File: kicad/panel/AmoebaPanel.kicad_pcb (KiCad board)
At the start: 2 copper layers, 127.8 x 100 mm, 204 parts, among them J1 Conn_01x01_Pin, J10 Conn_01x01_Pin, J11 Conn_01x01_Pin, J12 Conn_01x01_Pin, J13 Conn_01x01_Pin, J14 Conn_01x01_Pin, J15 Conn_01x01_Pin, J16 Conn_01x01_Pin, J17 Conn_01x01_Pin, J18 Conn_01x01_Pin, J19 Conn_01x01_Pin, J2 Conn_01x01_Pin, J20 Conn_01x01_Pin, J21 Conn_01x01_Pin, J22 Conn_01x01_Pin, J23 Conn_01x01_Pin, J24 Conn_01x01_Pin, J25 Conn_01x01_Pin, J26 Conn_01x01_Pin, J27 Conn_01x01_Pin, J28 Conn_01x01_Pin, J29 Conn_01x01_Pin, J3 Conn_01x01_Pin, J30 Conn_01x01_Pin, J31 Conn_01x01_Pin, J32 Conn_01x01_Pin, J33 Conn_01x01_Pin, J34 Conn_01x01_Pin, J35 Conn_01x01_Pin, J36 Conn_01x01_Pin, J37 Conn_01x01_Pin, J38 Conn_01x01_Pin, J39 Conn_01x01_Pin, J4 Conn_01x01_Pin, J40 Conn_01x01_Pin, J41 Conn_01x01_Pin, J42 Conn_01x01_Pin, J43 Conn_01x01_Pin, J44 Conn_01x01_Pin, J45 Conn_01x01_Pin, J46 Conn_01x01_Pin, J47 Conn_01x01_Pin, J48 Conn_01x01_Pin, J49 Conn_01x01_Pin, J5 Conn_01x01_Pin, J50 Conn_01x01_Pin, J51 Conn_01x01_Pin, J52 Conn_01x01_Pin, J53 Conn_01x01_Pin, J54 Conn_01x01_Pin, J55 Conn_01x01_Pin, J56 Conn_01x01_Pin, J57 Conn_01x01_Pin, J58 Conn_01x01_Pin, J59 Conn_01x01_Pin, J6 Conn_01x01_Pin, J60 Conn_01x01_Pin, J61 Conn_01x01_Pin, J62 Conn_01x01_Pin, J63 Conn_01x01_Pin, J64 Conn_01x01_Pin, J65 Conn_01x01_Pin, J66 Conn_01x01_Pin, J67 Conn_01x01_Pin, J68 Conn_01x01_Pin, J69 Conn_01x01_Pin, J7 Conn_01x01_Pin, J70 Conn_01x01_Pin, J71 Conn_01x01_Pin, J72 Conn_01x01_Pin, J73 Conn_01x01_Pin, J74 Conn_01x01_Pin, J75 Conn_01x01_Pin, J76 Conn_01x01_Pin, J77 Conn_01x01_Pin, J78 Conn_01x01_Pin, J79 Conn_01x01_Pin, J8 Conn_01x01_Pin, J80 Conn_01x01_Pin, J81 Conn_01x01_Pin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

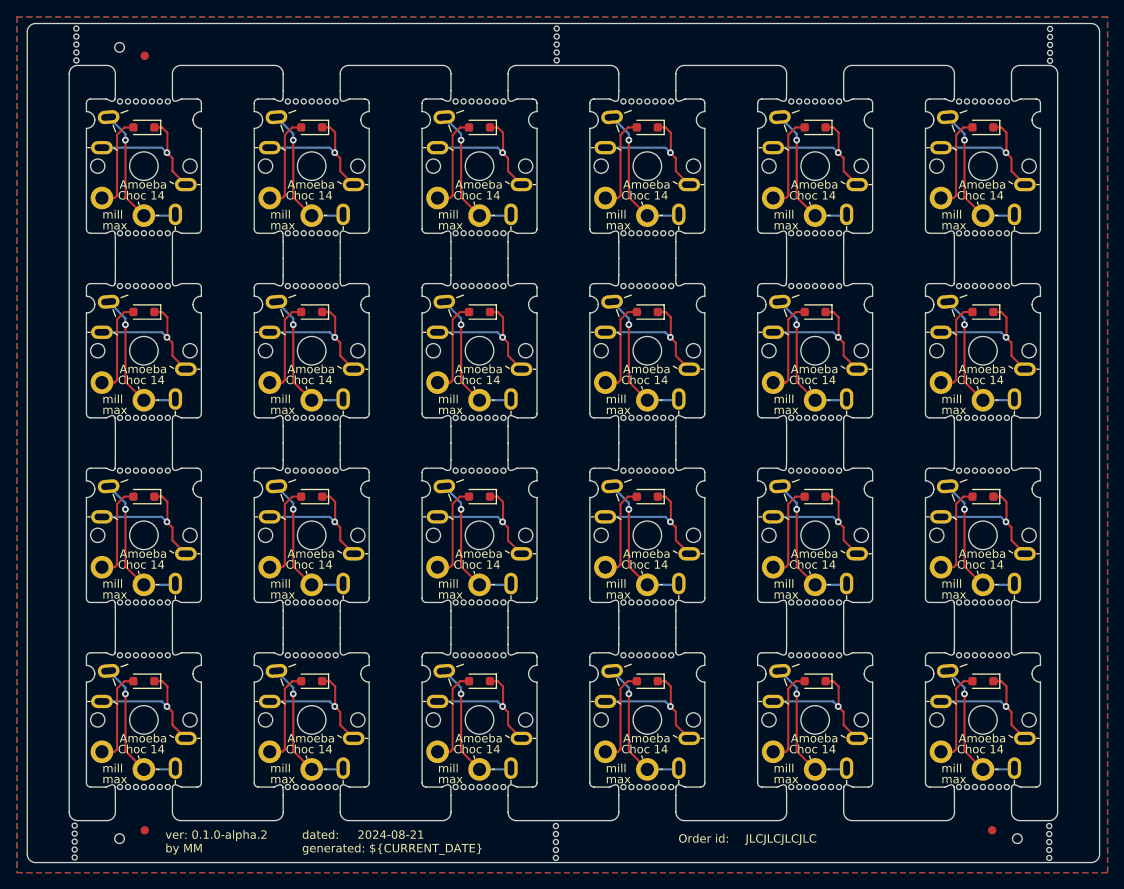
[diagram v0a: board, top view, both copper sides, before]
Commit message: feat(panel): better wording, move tooling holes
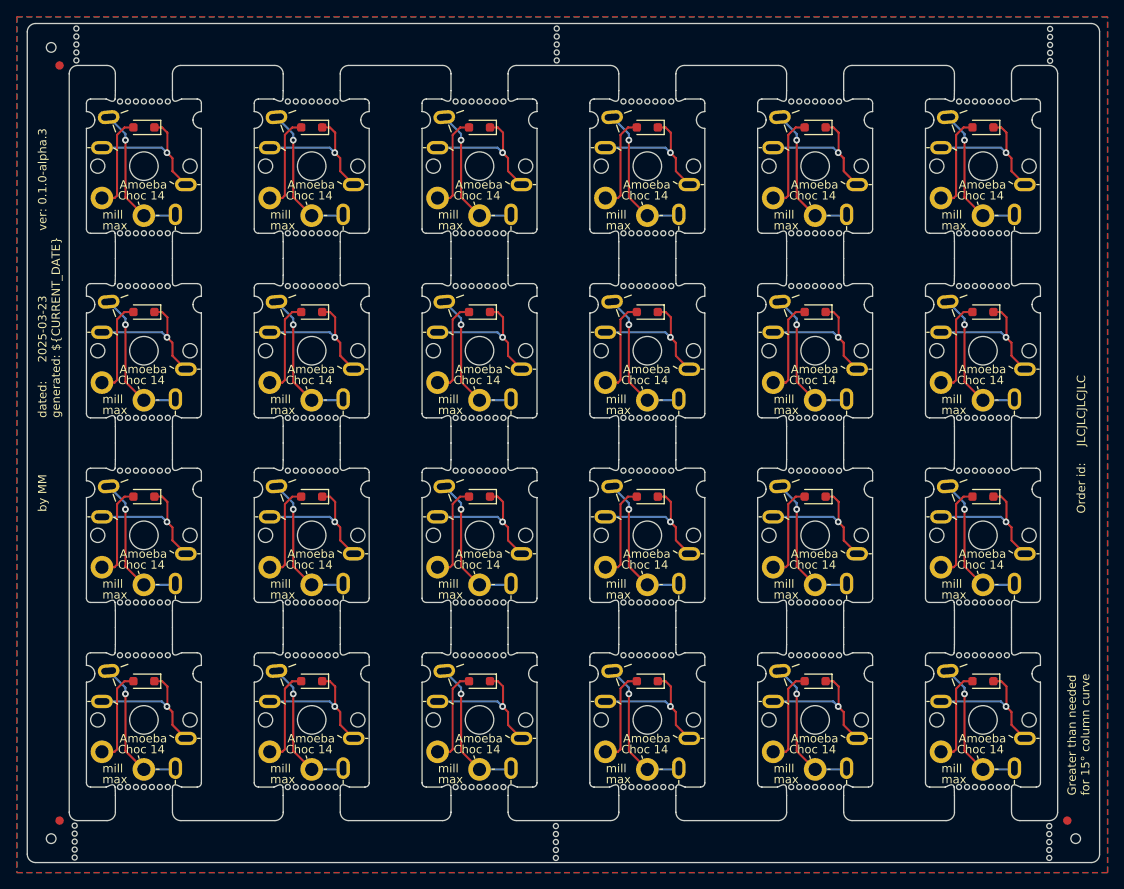
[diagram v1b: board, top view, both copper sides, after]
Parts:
- moved REF** 10.2 mm to (99.1, 55.8)
- moved REF** 10.2 mm to (99.1, 145.8)
- moved REF** 9.02 mm to (219.2, 145.8)
- moved ? 8.15 mm to (98.1, 147.9)
- moved ? 8.15 mm to (98.1, 53.6)
- moved ? 6.95 mm to (220.2, 147.9)
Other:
- board text added: "A typical 4 x 6 Dactyl wiring. Adjust for your board."
- board text added: "Greater than needed for 15° column curve"
- board text added: "Tidy"
- board text added: "by MM"
- board text added: "ver: ${REVISION}"
- board text added: "{dblquote}Tidy{dblquote} means curved and tidy. A little excess is safer, hence the curves."
- board text removed: "A typical 6 x 4 Dactyl wiring. Adjust for your board."
- board text removed: "Snug"
- board text removed: "ver: ${REVISION} by MM"

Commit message: feat(panel): re-insert Amoeba
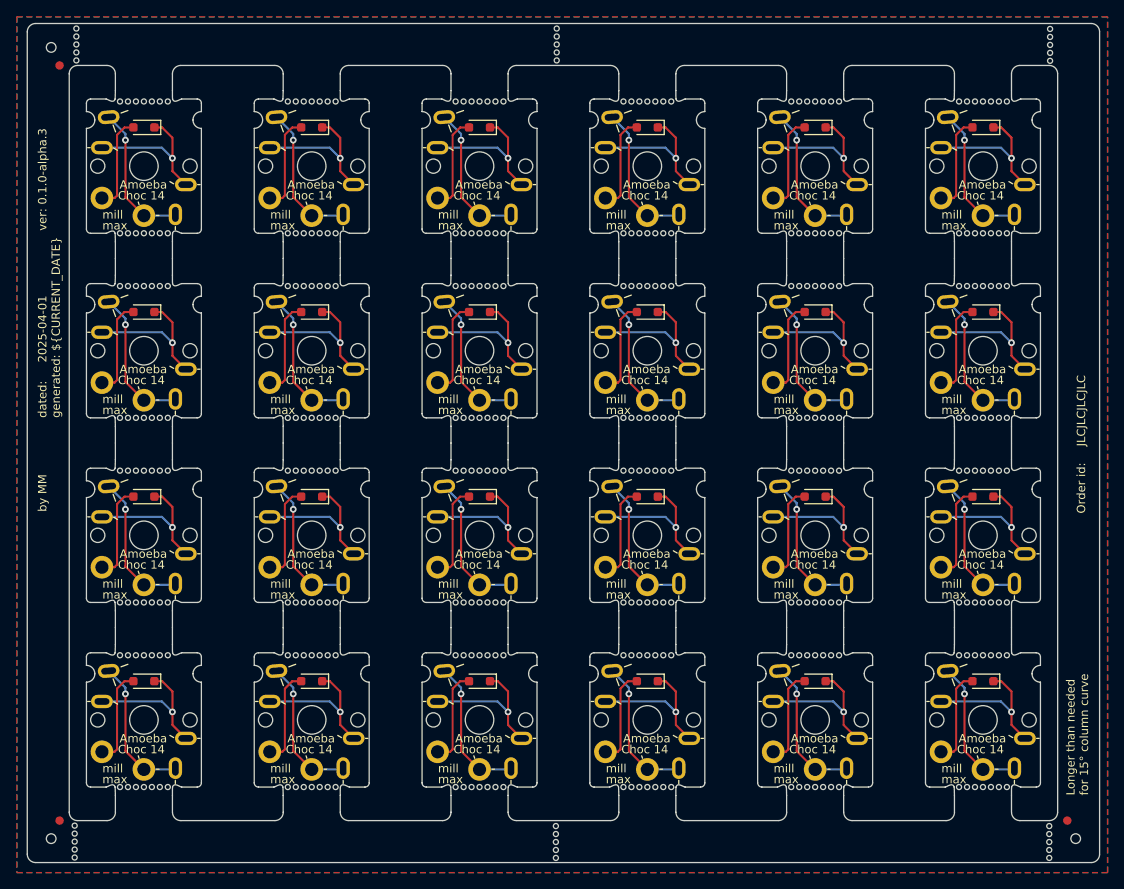
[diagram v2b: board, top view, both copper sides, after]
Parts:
- removed D10, D11, D12, D13, D14, D15, D16, D17, D18, D19, D2, D20, D21, D22, D23, D3, D4, D5, D6, D7, D8, D9: 1N4148, Diode_SMD:D_SOD-323_HandSoldering
- removed J10, J11, J12, J13, J14, J15, J16, J17, J18, J19, J20, J21, J22, J23, J24, J25, J26, J27, J28, J29, J30, J31, J32, J33, J34, J35, J36, J37, J38, J39, J40, J41, J42, J43, J44, J45, J46, J47, J48, J49, J5, J50, J51, J52, J53, J54, J55, J56, J57, J58, J59, J6, J60, J61, J62, J63, J64, J65, J66, J67, J68, J69, J7, J70, J71, J72, J73, J74, J75, J76, J77, J78, J79, J8, J80, J81, J82, J83, J84, J85, J86, J87, J88, J89, J9, J90, J91, J92: Conn_01x01_Pin, Amoeba_Choc_Nar:Pin_D0.8mm_L7.0mm
- removed REF**1, REF**10, REF**11, REF**12, REF**13, REF**14, REF**15, REF**16, REF**17, REF**18, REF**19, REF**2, REF**20, REF**21, REF**22, REF**23, REF**24, REF**25, REF**26, REF**27, REF**28, REF**29, REF**3, REF**30, REF**31, REF**32, REF**33, REF**34, REF**35, REF**36, REF**37, REF**38, REF**39, REF**4, REF**40, REF**41, REF**42, REF**43, REF**44, REF**5, REF**6, REF**7, REF**8, REF**9: Mouse_Bites, Amoeba_Choc_Nar:Mouse_Bites
- removed SW10, SW11, SW12, SW13, SW14, SW15, SW16, SW17, SW18, SW19, SW2, SW20, SW21, SW22, SW23, SW3, SW4, SW5, SW6, SW7, SW8, SW9: SW_SPST, Amoeba_Choc_Nar:pg1350-hotswap
- added D1: 1N4148, Diode_SMD:D_SOD-323_HandSoldering, F.Cu at (209.2, 129.2)
- added D1: 1N4148, Diode_SMD:D_SOD-323_HandSoldering, F.Cu at (209.2, 85.2)
- added D1: 1N4148, Diode_SMD:D_SOD-323_HandSoldering, F.Cu at (169.2, 129.2)
- added D1: 1N4148, Diode_SMD:D_SOD-323_HandSoldering, F.Cu at (149.2, 85.2)
- added D1: 1N4148, Diode_SMD:D_SOD-323_HandSoldering, F.Cu at (169.2, 107.2)
- added D1: 1N4148, Diode_SMD:D_SOD-323_HandSoldering, F.Cu at (189.2, 63.2)
- added D1: 1N4148, Diode_SMD:D_SOD-323_HandSoldering, F.Cu at (109.2, 107.2)
- added D1: 1N4148, Diode_SMD:D_SOD-323_HandSoldering, F.Cu at (129.2, 85.2)
- added D1: 1N4148, Diode_SMD:D_SOD-323_HandSoldering, F.Cu at (209.2, 63.2)
- added D1: 1N4148, Diode_SMD:D_SOD-323_HandSoldering, F.Cu at (169.2, 63.2)
- added D1: 1N4148, Diode_SMD:D_SOD-323_HandSoldering, F.Cu at (149.2, 129.2)
- added D1: 1N4148, Diode_SMD:D_SOD-323_HandSoldering, F.Cu at (109.2, 129.2)
- added D1: 1N4148, Diode_SMD:D_SOD-323_HandSoldering, F.Cu at (109.2, 85.2)
- added D1: 1N4148, Diode_SMD:D_SOD-323_HandSoldering, F.Cu at (209.2, 107.2)
- added D1: 1N4148, Diode_SMD:D_SOD-323_HandSoldering, F.Cu at (149.2, 63.2)
- added D1: 1N4148, Diode_SMD:D_SOD-323_HandSoldering, F.Cu at (149.2, 107.2)
- added D1: 1N4148, Diode_SMD:D_SOD-323_HandSoldering, F.Cu at (189.2, 107.2)
- added D1: 1N4148, Diode_SMD:D_SOD-323_HandSoldering, F.Cu at (169.2, 85.2)
- added D1: 1N4148, Diode_SMD:D_SOD-323_HandSoldering, F.Cu at (129.2, 107.2)
- added D1: 1N4148, Diode_SMD:D_SOD-323_HandSoldering, F.Cu at (129.2, 129.2)
- added D1: 1N4148, Diode_SMD:D_SOD-323_HandSoldering, F.Cu at (189.2, 85.2)
- added D1: 1N4148, Diode_SMD:D_SOD-323_HandSoldering, F.Cu at (189.2, 129.2)
- added J1: Conn_01x01_Pin, Amoeba_Choc_Nar:Pin_D0.8mm_L7.0mm, B.Cu at (144.9, 128.0)
- added J1: Conn_01x01_Pin, Amoeba_Choc_Nar:Pin_D0.8mm_L7.0mm, B.Cu at (184.9, 128.0)
- added J1: Conn_01x01_Pin, Amoeba_Choc_Nar:Pin_D0.8mm_L7.0mm, B.Cu at (105.0, 106.0)
- added J1: Conn_01x01_Pin, Amoeba_Choc_Nar:Pin_D0.8mm_L7.0mm, B.Cu at (125.0, 84.0)
- added J1: Conn_01x01_Pin, Amoeba_Choc_Nar:Pin_D0.8mm_L7.0mm, B.Cu at (184.9, 84.0)
- added J1: Conn_01x01_Pin, Amoeba_Choc_Nar:Pin_D0.8mm_L7.0mm, B.Cu at (204.9, 84.0)
- added J1: Conn_01x01_Pin, Amoeba_Choc_Nar:Pin_D0.8mm_L7.0mm, B.Cu at (164.9, 84.0)
- added J1: Conn_01x01_Pin, Amoeba_Choc_Nar:Pin_D0.8mm_L7.0mm, B.Cu at (204.9, 62.0)
- added J1: Conn_01x01_Pin, Amoeba_Choc_Nar:Pin_D0.8mm_L7.0mm, B.Cu at (105.0, 84.0)
- added J1: Conn_01x01_Pin, Amoeba_Choc_Nar:Pin_D0.8mm_L7.0mm, B.Cu at (184.9, 62.0)
- added J1: Conn_01x01_Pin, Amoeba_Choc_Nar:Pin_D0.8mm_L7.0mm, B.Cu at (204.9, 128.0)
- added J1: Conn_01x01_Pin, Amoeba_Choc_Nar:Pin_D0.8mm_L7.0mm, B.Cu at (164.9, 128.0)
- added J1: Conn_01x01_Pin, Amoeba_Choc_Nar:Pin_D0.8mm_L7.0mm, B.Cu at (164.9, 62.0)
- added J1: Conn_01x01_Pin, Amoeba_Choc_Nar:Pin_D0.8mm_L7.0mm, B.Cu at (105.0, 128.0)
- added J1: Conn_01x01_Pin, Amoeba_Choc_Nar:Pin_D0.8mm_L7.0mm, B.Cu at (164.9, 106.0)
- added J1: Conn_01x01_Pin, Amoeba_Choc_Nar:Pin_D0.8mm_L7.0mm, B.Cu at (184.9, 106.0)
- added J1: Conn_01x01_Pin, Amoeba_Choc_Nar:Pin_D0.8mm_L7.0mm, B.Cu at (144.9, 84.0)
- added J1: Conn_01x01_Pin, Amoeba_Choc_Nar:Pin_D0.8mm_L7.0mm, B.Cu at (125.0, 128.0)
- added J1: Conn_01x01_Pin, Amoeba_Choc_Nar:Pin_D0.8mm_L7.0mm, B.Cu at (144.9, 62.0)
- added J1: Conn_01x01_Pin, Amoeba_Choc_Nar:Pin_D0.8mm_L7.0mm, B.Cu at (125.0, 106.0)
- added J1: Conn_01x01_Pin, Amoeba_Choc_Nar:Pin_D0.8mm_L7.0mm, B.Cu at (144.9, 106.0)
- added J1: Conn_01x01_Pin, Amoeba_Choc_Nar:Pin_D0.8mm_L7.0mm, B.Cu at (204.9, 106.0)
- added J2: Conn_01x01_Pin, Amoeba_Choc_Nar:Pin_D0.8mm_L7.0mm, B.Cu at (172.9, 139.6)
- added J2: Conn_01x01_Pin, Amoeba_Choc_Nar:Pin_D0.8mm_L7.0mm, B.Cu at (112.9, 117.5)
- added J2: Conn_01x01_Pin, Amoeba_Choc_Nar:Pin_D0.8mm_L7.0mm, B.Cu at (192.9, 73.5)
- added J2: Conn_01x01_Pin, Amoeba_Choc_Nar:Pin_D0.8mm_L7.0mm, B.Cu at (212.9, 95.5)
- added J2: Conn_01x01_Pin, Amoeba_Choc_Nar:Pin_D0.8mm_L7.0mm, B.Cu at (132.9, 95.5)
- added J2: Conn_01x01_Pin, Amoeba_Choc_Nar:Pin_D0.8mm_L7.0mm, B.Cu at (212.9, 73.5)
- added J2: Conn_01x01_Pin, Amoeba_Choc_Nar:Pin_D0.8mm_L7.0mm, B.Cu at (152.9, 117.5)
- added J2: Conn_01x01_Pin, Amoeba_Choc_Nar:Pin_D0.8mm_L7.0mm, B.Cu at (192.9, 95.5)
- added J2: Conn_01x01_Pin, Amoeba_Choc_Nar:Pin_D0.8mm_L7.0mm, B.Cu at (192.9, 117.5)
- added J2: Conn_01x01_Pin, Amoeba_Choc_Nar:Pin_D0.8mm_L7.0mm, B.Cu at (152.9, 95.5)
- added J2: Conn_01x01_Pin, Amoeba_Choc_Nar:Pin_D0.8mm_L7.0mm, B.Cu at (172.9, 117.5)
- added J2: Conn_01x01_Pin, Amoeba_Choc_Nar:Pin_D0.8mm_L7.0mm, B.Cu at (152.9, 73.5)
- added J2: Conn_01x01_Pin, Amoeba_Choc_Nar:Pin_D0.8mm_L7.0mm, B.Cu at (152.9, 139.6)
- added J2: Conn_01x01_Pin, Amoeba_Choc_Nar:Pin_D0.8mm_L7.0mm, B.Cu at (172.9, 73.5)
- added J2: Conn_01x01_Pin, Amoeba_Choc_Nar:Pin_D0.8mm_L7.0mm, B.Cu at (192.9, 139.6)
- added J2: Conn_01x01_Pin, Amoeba_Choc_Nar:Pin_D0.8mm_L7.0mm, B.Cu at (172.9, 95.5)
- added J2: Conn_01x01_Pin, Amoeba_Choc_Nar:Pin_D0.8mm_L7.0mm, B.Cu at (212.9, 117.5)
- added J2: Conn_01x01_Pin, Amoeba_Choc_Nar:Pin_D0.8mm_L7.0mm, B.Cu at (112.9, 139.6)
- added J2: Conn_01x01_Pin, Amoeba_Choc_Nar:Pin_D0.8mm_L7.0mm, B.Cu at (212.9, 139.6)
- added J2: Conn_01x01_Pin, Amoeba_Choc_Nar:Pin_D0.8mm_L7.0mm, B.Cu at (112.9, 95.5)
- added J2: Conn_01x01_Pin, Amoeba_Choc_Nar:Pin_D0.8mm_L7.0mm, B.Cu at (132.9, 117.5)
- added J2: Conn_01x01_Pin, Amoeba_Choc_Nar:Pin_D0.8mm_L7.0mm, B.Cu at (132.9, 139.6)
- added J3: Conn_01x01_Pin, Amoeba_Choc_Nar:Pin_D0.8mm_L7.0mm, B.Cu at (184.2, 131.6)
- added J3: Conn_01x01_Pin, Amoeba_Choc_Nar:Pin_D0.8mm_L7.0mm, B.Cu at (164.2, 65.6)
- added J3: Conn_01x01_Pin, Amoeba_Choc_Nar:Pin_D0.8mm_L7.0mm, B.Cu at (144.2, 109.6)
- added J3: Conn_01x01_Pin, Amoeba_Choc_Nar:Pin_D0.8mm_L7.0mm, B.Cu at (204.2, 65.6)
- added J3: Conn_01x01_Pin, Amoeba_Choc_Nar:Pin_D0.8mm_L7.0mm, B.Cu at (164.2, 87.6)
- added J3: Conn_01x01_Pin, Amoeba_Choc_Nar:Pin_D0.8mm_L7.0mm, B.Cu at (124.2, 131.6)
- added J3: Conn_01x01_Pin, Amoeba_Choc_Nar:Pin_D0.8mm_L7.0mm, B.Cu at (184.2, 87.6)
- added J3: Conn_01x01_Pin, Amoeba_Choc_Nar:Pin_D0.8mm_L7.0mm, B.Cu at (164.2, 109.6)
- added J3: Conn_01x01_Pin, Amoeba_Choc_Nar:Pin_D0.8mm_L7.0mm, B.Cu at (184.2, 65.6)
- added J3: Conn_01x01_Pin, Amoeba_Choc_Nar:Pin_D0.8mm_L7.0mm, B.Cu at (144.2, 131.6)
- added J3: Conn_01x01_Pin, Amoeba_Choc_Nar:Pin_D0.8mm_L7.0mm, B.Cu at (144.2, 87.6)
- added J3: Conn_01x01_Pin, Amoeba_Choc_Nar:Pin_D0.8mm_L7.0mm, B.Cu at (184.2, 109.6)
- added J3: Conn_01x01_Pin, Amoeba_Choc_Nar:Pin_D0.8mm_L7.0mm, B.Cu at (164.2, 131.6)
- added J3: Conn_01x01_Pin, Amoeba_Choc_Nar:Pin_D0.8mm_L7.0mm, B.Cu at (104.2, 109.6)
- added J3: Conn_01x01_Pin, Amoeba_Choc_Nar:Pin_D0.8mm_L7.0mm, B.Cu at (124.2, 87.6)
- added J3: Conn_01x01_Pin, Amoeba_Choc_Nar:Pin_D0.8mm_L7.0mm, B.Cu at (204.2, 131.6)
- added J3: Conn_01x01_Pin, Amoeba_Choc_Nar:Pin_D0.8mm_L7.0mm, B.Cu at (204.2, 87.6)
- added J3: Conn_01x01_Pin, Amoeba_Choc_Nar:Pin_D0.8mm_L7.0mm, B.Cu at (104.2, 131.6)
- added J3: Conn_01x01_Pin, Amoeba_Choc_Nar:Pin_D0.8mm_L7.0mm, B.Cu at (144.2, 65.6)
- added J3: Conn_01x01_Pin, Amoeba_Choc_Nar:Pin_D0.8mm_L7.0mm, B.Cu at (104.2, 87.6)
- added J3: Conn_01x01_Pin, Amoeba_Choc_Nar:Pin_D0.8mm_L7.0mm, B.Cu at (204.2, 109.6)
- added J3: Conn_01x01_Pin, Amoeba_Choc_Nar:Pin_D0.8mm_L7.0mm, B.Cu at (124.2, 109.6)
- added J4: Conn_01x01_Pin, Amoeba_Choc_Nar:Pin_D0.8mm_L7.0mm, B.Cu at (174.2, 136.0)
- added J4: Conn_01x01_Pin, Amoeba_Choc_Nar:Pin_D0.8mm_L7.0mm, B.Cu at (134.2, 114.0)
- added J4: Conn_01x01_Pin, Amoeba_Choc_Nar:Pin_D0.8mm_L7.0mm, B.Cu at (214.2, 136.0)
- added J4: Conn_01x01_Pin, Amoeba_Choc_Nar:Pin_D0.8mm_L7.0mm, B.Cu at (214.2, 92.0)
- added J4: Conn_01x01_Pin, Amoeba_Choc_Nar:Pin_D0.8mm_L7.0mm, B.Cu at (154.2, 114.0)
- added J4: Conn_01x01_Pin, Amoeba_Choc_Nar:Pin_D0.8mm_L7.0mm, B.Cu at (154.2, 136.0)
- added J4: Conn_01x01_Pin, Amoeba_Choc_Nar:Pin_D0.8mm_L7.0mm, B.Cu at (154.2, 70.0)
- added J4: Conn_01x01_Pin, Amoeba_Choc_Nar:Pin_D0.8mm_L7.0mm, B.Cu at (194.2, 114.0)
- added J4: Conn_01x01_Pin, Amoeba_Choc_Nar:Pin_D0.8mm_L7.0mm, B.Cu at (214.2, 70.0)
- added J4: Conn_01x01_Pin, Amoeba_Choc_Nar:Pin_D0.8mm_L7.0mm, B.Cu at (154.2, 92.0)
- added J4: Conn_01x01_Pin, Amoeba_Choc_Nar:Pin_D0.8mm_L7.0mm, B.Cu at (114.2, 136.0)
- added J4: Conn_01x01_Pin, Amoeba_Choc_Nar:Pin_D0.8mm_L7.0mm, B.Cu at (174.2, 92.0)
- added J4: Conn_01x01_Pin, Amoeba_Choc_Nar:Pin_D0.8mm_L7.0mm, B.Cu at (134.2, 92.0)
- added J4: Conn_01x01_Pin, Amoeba_Choc_Nar:Pin_D0.8mm_L7.0mm, B.Cu at (174.2, 114.0)
- added J4: Conn_01x01_Pin, Amoeba_Choc_Nar:Pin_D0.8mm_L7.0mm, B.Cu at (174.2, 70.0)
- added J4: Conn_01x01_Pin, Amoeba_Choc_Nar:Pin_D0.8mm_L7.0mm, B.Cu at (114.2, 92.0)
- added J4: Conn_01x01_Pin, Amoeba_Choc_Nar:Pin_D0.8mm_L7.0mm, B.Cu at (114.2, 114.0)
- added J4: Conn_01x01_Pin, Amoeba_Choc_Nar:Pin_D0.8mm_L7.0mm, B.Cu at (194.2, 70.0)
- added J4: Conn_01x01_Pin, Amoeba_Choc_Nar:Pin_D0.8mm_L7.0mm, B.Cu at (214.2, 114.0)
- added J4: Conn_01x01_Pin, Amoeba_Choc_Nar:Pin_D0.8mm_L7.0mm, B.Cu at (194.2, 136.0)
- added J4: Conn_01x01_Pin, Amoeba_Choc_Nar:Pin_D0.8mm_L7.0mm, B.Cu at (194.2, 92.0)
- added J4: Conn_01x01_Pin, Amoeba_Choc_Nar:Pin_D0.8mm_L7.0mm, B.Cu at (134.2, 136.0)
- added REF**: Mouse_Bites, Amoeba_Choc_Nar:Mouse_Bites, F.Cu at (109.2, 82.1)
- added REF**: Mouse_Bites, Amoeba_Choc_Nar:Mouse_Bites, F.Cu at (149.2, 75.8)
- added REF**: Mouse_Bites, Amoeba_Choc_Nar:Mouse_Bites, F.Cu at (169.2, 141.8)
- added REF**: Mouse_Bites, Amoeba_Choc_Nar:Mouse_Bites, F.Cu at (129.2, 141.8)
- added REF**: Mouse_Bites, Amoeba_Choc_Nar:Mouse_Bites, F.Cu at (109.2, 97.8)
- added REF**: Mouse_Bites, Amoeba_Choc_Nar:Mouse_Bites, F.Cu at (169.2, 75.8)
- added REF**: Mouse_Bites, Amoeba_Choc_Nar:Mouse_Bites, F.Cu at (149.2, 141.8)
- added REF**: Mouse_Bites, Amoeba_Choc_Nar:Mouse_Bites, F.Cu at (209.2, 104.1)
- added REF**: Mouse_Bites, Amoeba_Choc_Nar:Mouse_Bites, F.Cu at (209.2, 60.1)
- added REF**: Mouse_Bites, Amoeba_Choc_Nar:Mouse_Bites, F.Cu at (189.2, 97.8)
- added REF**: Mouse_Bites, Amoeba_Choc_Nar:Mouse_Bites, F.Cu at (189.2, 60.1)
- added REF**: Mouse_Bites, Amoeba_Choc_Nar:Mouse_Bites, F.Cu at (189.2, 75.8)
- added REF**: Mouse_Bites, Amoeba_Choc_Nar:Mouse_Bites, F.Cu at (169.2, 82.1)
- added REF**: Mouse_Bites, Amoeba_Choc_Nar:Mouse_Bites, F.Cu at (209.2, 75.8)
- added REF**: Mouse_Bites, Amoeba_Choc_Nar:Mouse_Bites, F.Cu at (149.2, 60.1)
- added REF**: Mouse_Bites, Amoeba_Choc_Nar:Mouse_Bites, F.Cu at (129.2, 119.8)
- added REF**: Mouse_Bites, Amoeba_Choc_Nar:Mouse_Bites, F.Cu at (129.2, 82.1)
- added REF**: Mouse_Bites, Amoeba_Choc_Nar:Mouse_Bites, F.Cu at (109.2, 126.1)
- added REF**: Mouse_Bites, Amoeba_Choc_Nar:Mouse_Bites, F.Cu at (169.2, 126.1)
- added REF**: Mouse_Bites, Amoeba_Choc_Nar:Mouse_Bites, F.Cu at (129.2, 97.8)
- added REF**: Mouse_Bites, Amoeba_Choc_Nar:Mouse_Bites, F.Cu at (109.2, 141.8)
- added REF**: Mouse_Bites, Amoeba_Choc_Nar:Mouse_Bites, F.Cu at (209.2, 97.8)
- added REF**: Mouse_Bites, Amoeba_Choc_Nar:Mouse_Bites, F.Cu at (149.2, 97.8)
- added REF**: Mouse_Bites, Amoeba_Choc_Nar:Mouse_Bites, F.Cu at (149.2, 126.1)
- added REF**: Mouse_Bites, Amoeba_Choc_Nar:Mouse_Bites, F.Cu at (189.2, 141.8)
- added REF**: Mouse_Bites, Amoeba_Choc_Nar:Mouse_Bites, F.Cu at (129.2, 126.1)
- added REF**: Mouse_Bites, Amoeba_Choc_Nar:Mouse_Bites, F.Cu at (149.2, 82.1)
- added REF**: Mouse_Bites, Amoeba_Choc_Nar:Mouse_Bites, F.Cu at (189.2, 119.8)
- added REF**: Mouse_Bites, Amoeba_Choc_Nar:Mouse_Bites, F.Cu at (189.2, 126.1)
- added REF**: Mouse_Bites, Amoeba_Choc_Nar:Mouse_Bites, F.Cu at (169.2, 60.1)
- added REF**: Mouse_Bites, Amoeba_Choc_Nar:Mouse_Bites, F.Cu at (209.2, 119.8)
- added REF**: Mouse_Bites, Amoeba_Choc_Nar:Mouse_Bites, F.Cu at (129.2, 104.1)
- added REF**: Mouse_Bites, Amoeba_Choc_Nar:Mouse_Bites, F.Cu at (149.2, 119.8)
- added REF**: Mouse_Bites, Amoeba_Choc_Nar:Mouse_Bites, F.Cu at (109.2, 104.1)
- added REF**: Mouse_Bites, Amoeba_Choc_Nar:Mouse_Bites, F.Cu at (169.2, 104.1)
- added REF**: Mouse_Bites, Amoeba_Choc_Nar:Mouse_Bites, F.Cu at (189.2, 82.1)
- added REF**: Mouse_Bites, Amoeba_Choc_Nar:Mouse_Bites, F.Cu at (169.2, 119.8)
- added REF**: Mouse_Bites, Amoeba_Choc_Nar:Mouse_Bites, F.Cu at (189.2, 104.1)
- added REF**: Mouse_Bites, Amoeba_Choc_Nar:Mouse_Bites, F.Cu at (209.2, 141.8)
- added REF**: Mouse_Bites, Amoeba_Choc_Nar:Mouse_Bites, F.Cu at (109.2, 119.8)
- added REF**: Mouse_Bites, Amoeba_Choc_Nar:Mouse_Bites, F.Cu at (209.2, 126.1)
- added REF**: Mouse_Bites, Amoeba_Choc_Nar:Mouse_Bites, F.Cu at (209.2, 82.1)
- added REF**: Mouse_Bites, Amoeba_Choc_Nar:Mouse_Bites, F.Cu at (169.2, 97.8)
- added REF**: Mouse_Bites, Amoeba_Choc_Nar:Mouse_Bites, F.Cu at (149.2, 104.1)
- added SW1: SW_SPST, Amoeba_Choc_Nar:pg1350-hotswap, F.Cu at (109.2, 111.8)
- added SW1: SW_SPST, Amoeba_Choc_Nar:pg1350-hotswap, F.Cu at (149.2, 67.8)
- added SW1: SW_SPST, Amoeba_Choc_Nar:pg1350-hotswap, F.Cu at (189.2, 133.8)
- added SW1: SW_SPST, Amoeba_Choc_Nar:pg1350-hotswap, F.Cu at (209.2, 111.8)
- added SW1: SW_SPST, Amoeba_Choc_Nar:pg1350-hotswap, F.Cu at (169.2, 67.8)
- added SW1: SW_SPST, Amoeba_Choc_Nar:pg1350-hotswap, F.Cu at (209.2, 67.8)
- added SW1: SW_SPST, Amoeba_Choc_Nar:pg1350-hotswap, F.Cu at (149.2, 89.8)
- added SW1: SW_SPST, Amoeba_Choc_Nar:pg1350-hotswap, F.Cu at (129.2, 111.8)
- added SW1: SW_SPST, Amoeba_Choc_Nar:pg1350-hotswap, F.Cu at (129.2, 89.8)
- added SW1: SW_SPST, Amoeba_Choc_Nar:pg1350-hotswap, F.Cu at (169.2, 133.8)
- added SW1: SW_SPST, Amoeba_Choc_Nar:pg1350-hotswap, F.Cu at (189.2, 111.8)
- added SW1: SW_SPST, Amoeba_Choc_Nar:pg1350-hotswap, F.Cu at (109.2, 133.8)
- added SW1: SW_SPST, Amoeba_Choc_Nar:pg1350-hotswap, F.Cu at (189.2, 89.8)
- added SW1: SW_SPST, Amoeba_Choc_Nar:pg1350-hotswap, F.Cu at (109.2, 89.8)
- added SW1: SW_SPST, Amoeba_Choc_Nar:pg1350-hotswap, F.Cu at (169.2, 111.8)
- added SW1: SW_SPST, Amoeba_Choc_Nar:pg1350-hotswap, F.Cu at (149.2, 111.8)
- added SW1: SW_SPST, Amoeba_Choc_Nar:pg1350-hotswap, F.Cu at (209.2, 89.8)
- added SW1: SW_SPST, Amoeba_Choc_Nar:pg1350-hotswap, F.Cu at (149.2, 133.8)
- added SW1: SW_SPST, Amoeba_Choc_Nar:pg1350-hotswap, F.Cu at (129.2, 133.8)
- added SW1: SW_SPST, Amoeba_Choc_Nar:pg1350-hotswap, F.Cu at (189.2, 67.8)
- added SW1: SW_SPST, Amoeba_Choc_Nar:pg1350-hotswap, F.Cu at (209.2, 133.8)
- added SW1: SW_SPST, Amoeba_Choc_Nar:pg1350-hotswap, F.Cu at (169.2, 89.8)
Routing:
- net /row: track 401.9 -> 423.0 mm
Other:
- board text added: "Longer than needed for 15° column curve"
- board text added: "v010a3"
- board text added: "{dblquote}Tidy{dblquote} means curved and neat. A little excess is safer, hence the curves."
- board text removed: "Greater than needed for 15° column curve"
- board text removed: "v010a2"
- board text removed: "{dblquote}Tidy{dblquote} means curved and tidy. A little excess is safer, hence the curves."
